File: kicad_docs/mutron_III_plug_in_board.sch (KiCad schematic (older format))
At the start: 46 parts, among them J1 Conn_01x04_Male, J2 Conn_01x04_Male, J3 Conn_01x04_Male, J4 Conn_01x08_Male, J5 HP-BP-LP, Q1 BC857, Q2 BCM847, Q3 BC847, U1 TL072, U2 RC4558, U3 vactrol, U4 vactrol, U5 RC4558

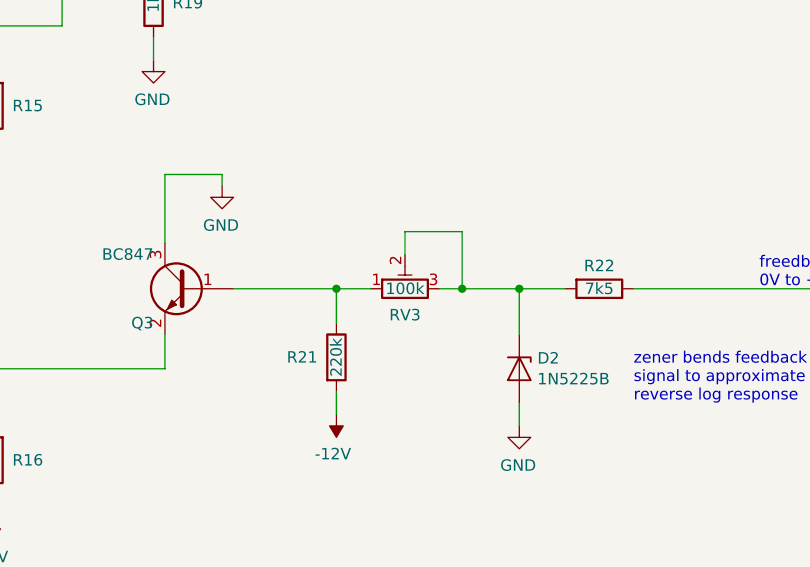
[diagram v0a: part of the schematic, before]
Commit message: change trimmers to cheaper TH type
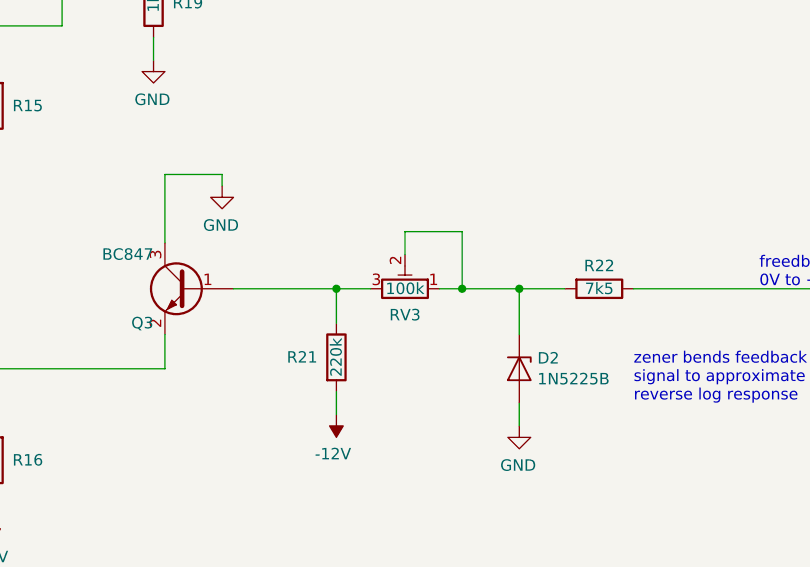
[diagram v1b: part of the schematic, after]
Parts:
- RV1, RV2, RV3: footprint Potentiometer_SMD:Potentiometer_Bourns_3269W_Vertical -> Potentiometer_THT:Potentiometer_Bourns_3296W_Vertical
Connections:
- net at Q3.1 (B), R21.1: now also RV3.3; no longer RV3.1
- net at D2.1 (K), R22.2, RV3.2: now also RV3.1; no longer RV3.3
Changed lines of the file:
@@
 F 0 "RV1" H 2780 7354 50  0000 R CNN
 F 1 "10k" V 2850 7450 50  0000 R CNN
-F 2 "Potentiometer_SMD:Potentiometer_Bourns_3269W_Vertical" H 2850 7400 50  0001 C CNN
+F 2 "Potentiometer_THT:Potentiometer_Bourns_3296W_Vertical" H 2850 7400 50  0001 C CNN
 F 3 "~" H 2850 7400 50  0001 C CNN
 	1    2850 7400
@@
 F 0 "RV2" V 3085 8200 50  0000 C CNN
 F 1 "100k" V 3200 8200 50  0000 C CNN
-F 2 "Potentiometer_SMD:Potentiometer_Bourns_3269W_Vertical" H 3200 8200 50  0001 C CNN
+F 2 "Potentiometer_THT:Potentiometer_Bourns_3296W_Vertical" H 3200 8200 50  0001 C CNN
 F 3 "~" H 3200 8200 50  0001 C CNN
 	1    3200 8200
@@
 F 0 "RV3" V 9385 6500 50  0000 C CNN
 F 1 "100k" V 9500 6500 50  0000 C CNN
-F 2 "Potentiometer_SMD:Potentiometer_Bourns_3269W_Vertical" H 9500 6500 50  0001 C CNN
+F 2 "Potentiometer_THT:Potentiometer_Bourns_3296W_Vertical" H 9500 6500 50  0001 C CNN
 F 3 "~" H 9500 6500 50  0001 C CNN
 	1    9500 6500
-	0    -1   -1   0
-$EndComp
-$Comp
+	0    1    -1   0
+$EndComp
+$Comp
